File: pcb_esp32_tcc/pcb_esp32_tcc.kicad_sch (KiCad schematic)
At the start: 13 parts, among them J1 Screw_Terminal_01x03, J2 Screw_Terminal_01x03, J3 Screw_Terminal_01x03, J4 Screw_Terminal_01x03, J5 Conn_01x01_Pin, J6 Conn_01x01_Pin, Q1 NPN, U1 ESP32-DevKitC

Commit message: Update esp32 footprint and symbol
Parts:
- added J7: Conn_01x01_Pin, Connector_PinHeader_2.54mm:PinHeader_1x01_P2.54mm_Vertical, symbol Connector:Conn_01x01_Pin
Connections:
- net GND: now also J7.1 (Pin_1)
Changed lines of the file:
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@@
+	)
+	(junction
+		(at 81.28 105.41)
+		(diameter 0)
+		(color 0 0 0 0)
 	)
 	(junction
@@
 	(wire
 		(pts
+			(xy 72.39 105.41) (xy 81.28 105.41)
+		)
+		(stroke
+			(width 0)
+			(type default)
+		)
+	)
+	(wire
+		(pts
+			(xy 81.28 105.41) (xy 81.28 106.68)
+		)
+		(stroke
+			(width 0)
+			(type default)
+		)
+	)
+	(wire
+		(pts
 			(xy 250.19 129.54) (xy 250.19 132.08)
 		)
@@
 	(wire
 		(pts
-			(xy 81.28 104.14) (xy 81.28 106.68)
+			(xy 81.28 104.14) (xy 81.28 105.41)
 		)
 		(stroke
@@
 		)
 	)
+	(symbol
+		(lib_id "Connector:Conn_01x01_Pin")
+		(at 67.31 105.41 0)
+		(unit 1)
+		(exclude_from_sim no)
+		(in_bom yes)
+		(on_board yes)
+		(dnp no)
+		(fields_autoplaced yes)
+		(property "Reference" "J7"
+			(at 67.945 100.33 0)
+			(effects
+				(font
+					(size 1.27 1.27)
+				)
+			)
+		)
+		(property "Value" "Conn_01x01_Pin"
+			(at 67.945 102.87 0)
+			(effects
+				(font
+					(size 1.27 1.27)
+				)
+			)
+		)
+		(property "Footprint" "Connector_PinHeader_2.54mm:PinHeader_1x01_P2.54mm_Vertical"
+			(at 67.31 105.41 0)
+			(effects
+				(font
+					(size 1.27 1.27)
+				)
+				(hide yes)
+			)
+		)
+		(property "Datasheet" "~"
+			(at 67.31 105.41 0)
+			(effects
+				(font
+					(size 1.27 1.27)
+				)
+				(hide yes)
+			)
+		)
+		(property "Description" "Generic connector, single row, 01x01, script generated"
+			(at 67.31 105.41 0)
+			(effects
+				(font
+					(size 1.27 1.27)
+				)
+				(hide yes)
+			)
+		)
+		(pin "1"
+		)
+		(instances
+			(project "pcb_esp32_tcc"
+				(path "/99d18d59-4c06-40b2-add7-d919244a681a"
+					(reference "J7")
+					(unit 1)
+				)
+			)
+		)
+	)

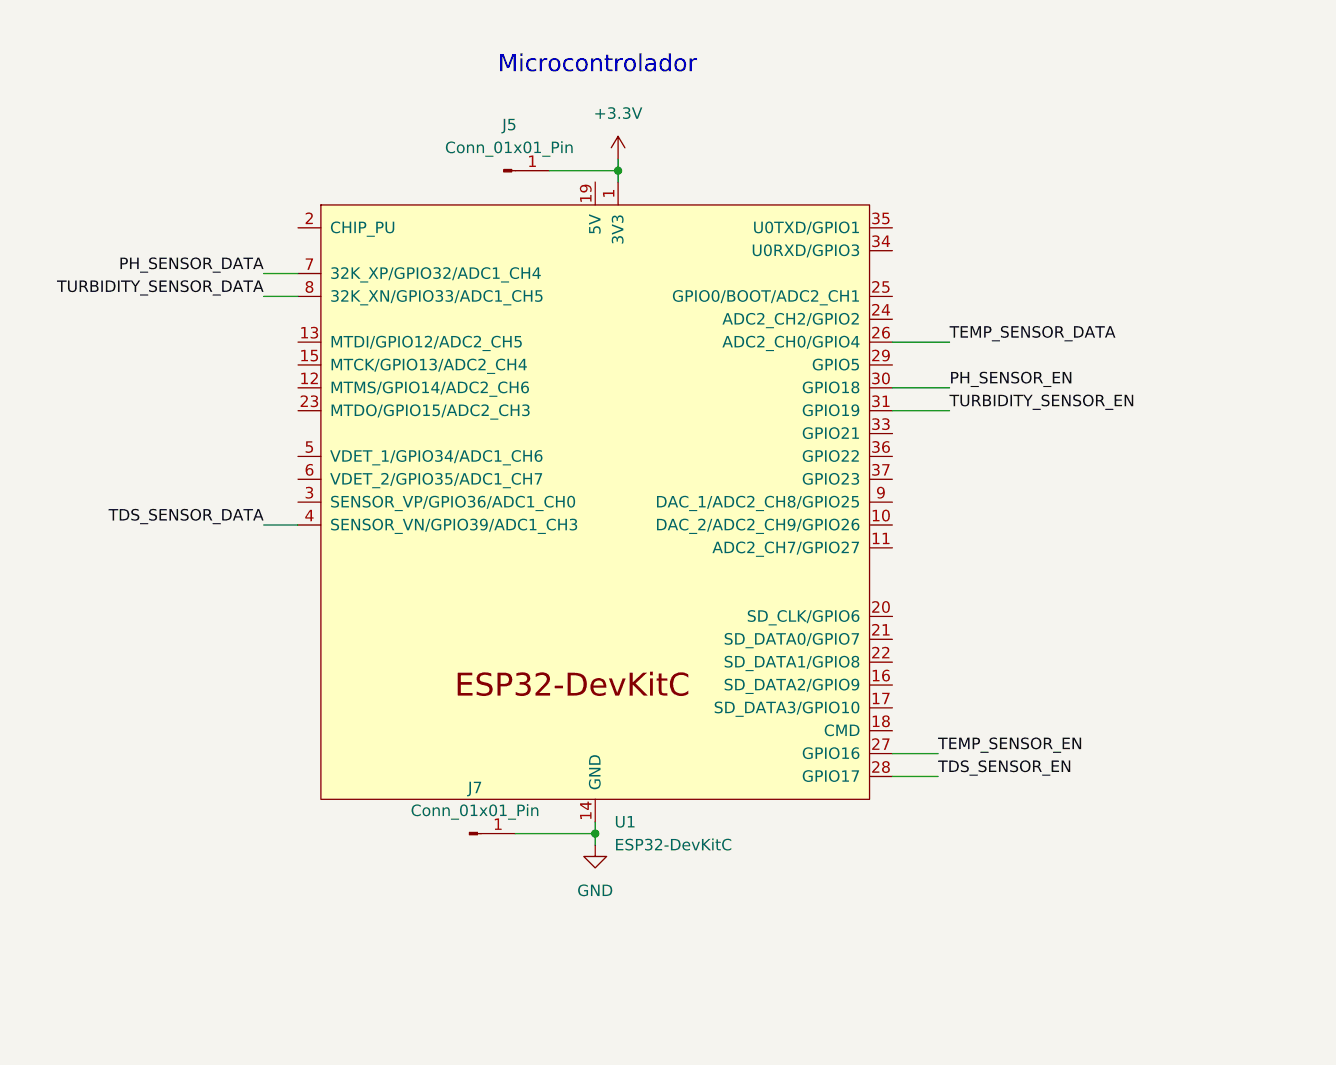
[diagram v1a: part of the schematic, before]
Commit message: Update esp32 footprint and symbol
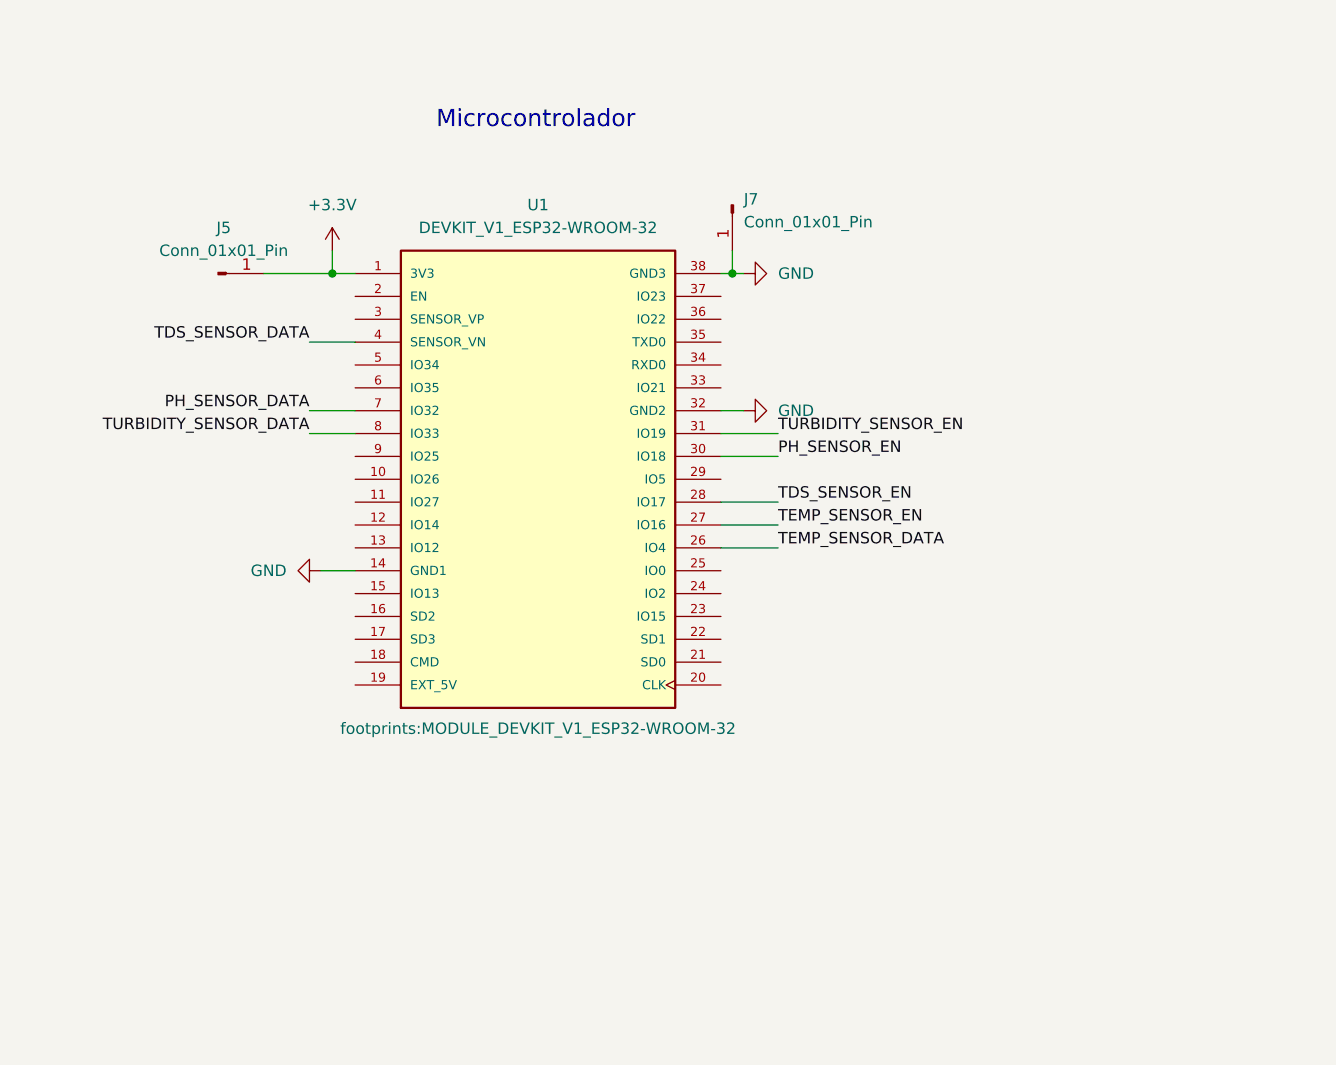
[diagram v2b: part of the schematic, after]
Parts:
- removed U1: ESP32-DevKitC, PCM_Espressif:ESP32-DevKitC, symbol PCM_Espressif:ESP32-DevKitC
- added U1: DEVKIT_V1_ESP32-WROOM-32, footprints:MODULE_DEVKIT_V1_ESP32-WROOM-32, symbol DEVKIT_V1_ESP32-WROOM-32:DEVKIT_V1_ESP32-WROOM-32
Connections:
- net +3.3V: now also U1.1 (3V3)
- net GND: now also U1.14 (GND1), U1.32 (GND2), U1.38 (GND3)
- net PH_SENSOR_DATA: now also U1.7 (IO32)
- net PH_SENSOR_EN: now also U1.30 (IO18)
- net TDS_SENSOR_DATA: now also U1.4 (SENSOR_VN)
- net TDS_SENSOR_EN: now also U1.28 (IO17)
- net TEMP_SENSOR_DATA: now also U1.26 (IO4)
- net TEMP_SENSOR_EN: now also U1.27 (IO16)
- net TURBIDITY_SENSOR_DATA: now also U1.8 (IO33)
- net TURBIDITY_SENSOR_EN: now also U1.31 (IO19)
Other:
- moved on the sheet: J5, J7
